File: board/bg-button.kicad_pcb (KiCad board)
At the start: 2 copper layers, 19.2 x 13 mm, 7 parts, among them SW1 SW_Push, U1 breakoutgarden_i2c

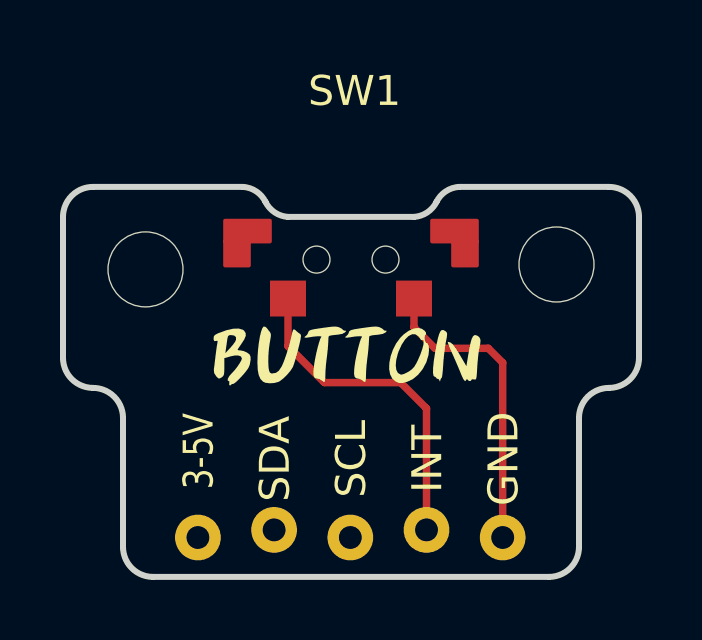
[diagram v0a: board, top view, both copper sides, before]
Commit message: Rev.2
* fix connector height
* fix through hole size
* fix mount hole position
* fix some silk designs
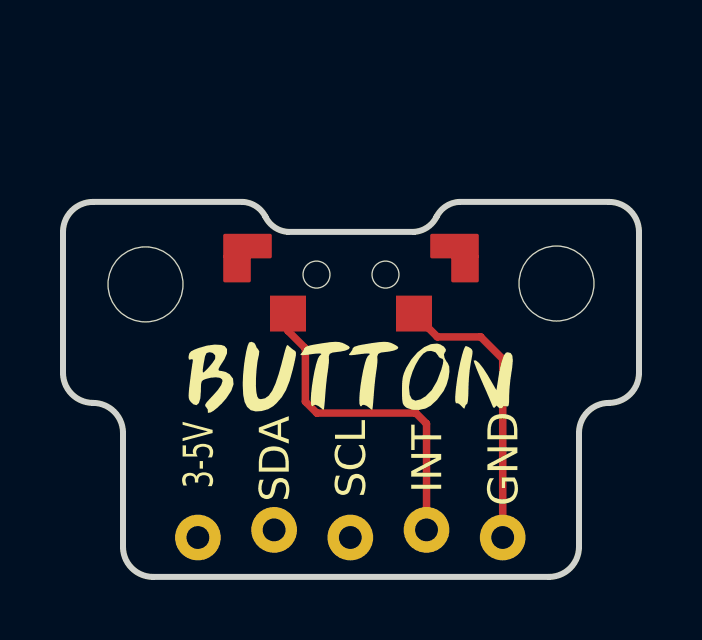
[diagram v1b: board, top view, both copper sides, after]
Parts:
- removed the G*** at (133.5, 119.6)
- removed the G*** at (133.6, 118.9)
- added G***: BUTTON-11mm, bg-button:button, F.Cu at (133.6, 120.3)
- added G***: LOGO_rev2, bg-button:logo-rev2, B.Cu at (133.6, 119.4)
- moved REF** 0.64 mm to (140.4, 117.2)
- moved REF** 0.50 mm to (126.8, 117.2)
- moved SW1 0.50 mm to (129.4, 115.6)
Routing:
- net GND: track 10.2 -> 9.56 mm
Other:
- board size 19.2 x 13 mm -> 19.2 x 12.5 mm
- board text added: "@Akkiesoft"
- board text removed: "https://8639.tk"
